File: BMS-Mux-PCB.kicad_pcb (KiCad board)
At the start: 2 copper layers, 113.5 x 88 mm, 54 parts, among them J1 Conn_02x08_Counter_Clockwise, J2 Conn_02x08_Counter_Clockwise, J3 Conn_02x09_Top_Bottom, J4 Conn_01x18, J5 Conn_01x02, J6 Conn_02x10_Odd_Even, Q1 BSS123, Q2 BSS123, U1 74CBTLV3257, U2 74CBTLV3257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

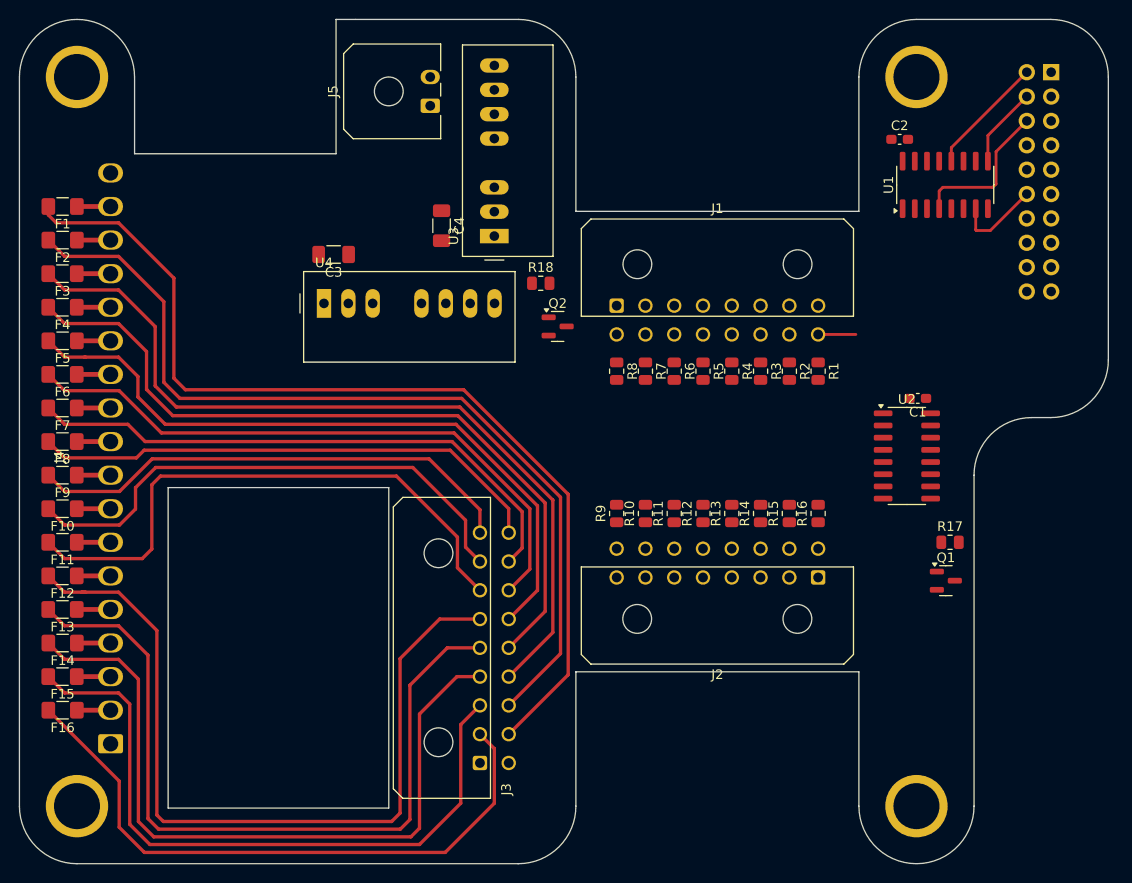
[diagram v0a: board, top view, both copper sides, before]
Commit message: changed connector orientation and halfway routed
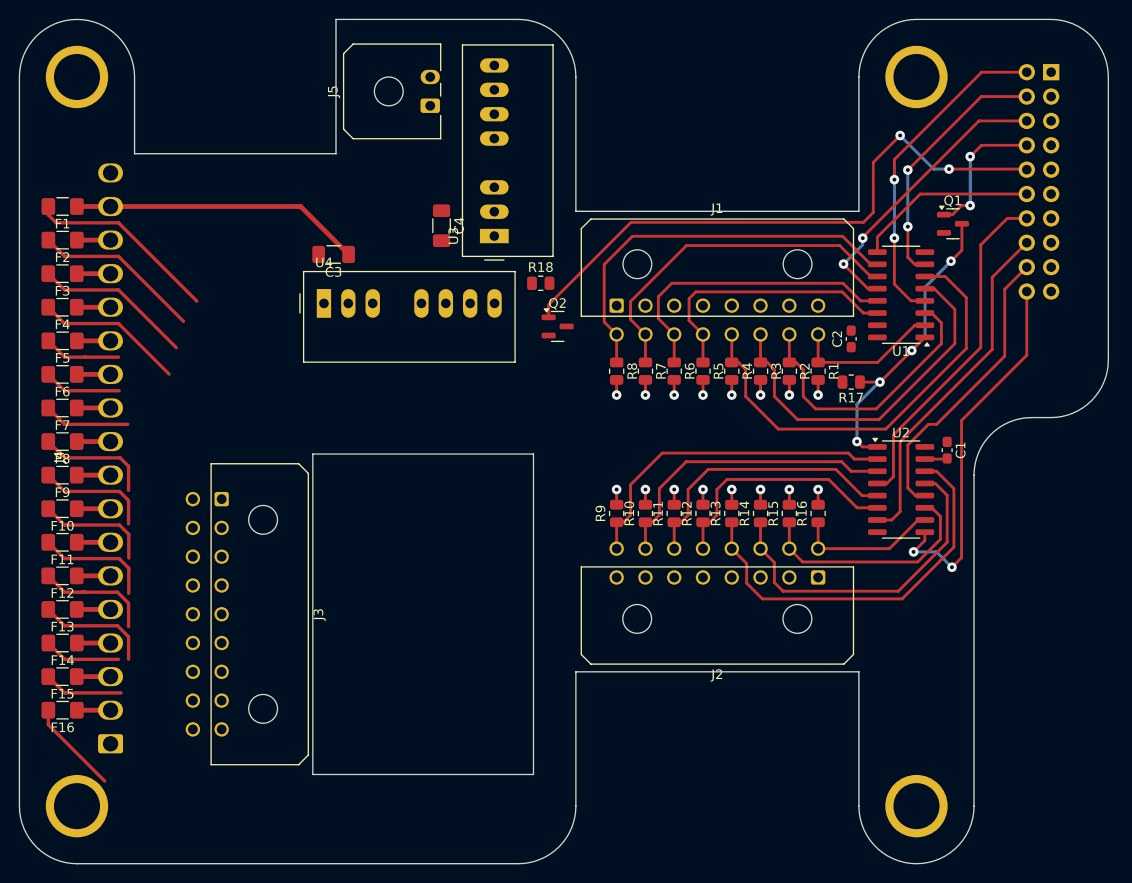
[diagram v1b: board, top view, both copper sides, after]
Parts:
- moved J3 38.5 mm to (85.6, 99.5), turned to -90 degrees
- moved Q1 37.2 mm to (161.8, 70.8)
- moved C2 21.4 mm to (151.2, 82.8), turned to 90 degrees
- moved R17 19.6 mm to (151.2, 87.3), turned to 180 degrees
- moved U1 12.3 mm to (156.4, 78.2), turned to 180 degrees
- moved C1 6.21 mm to (161.2, 94.4), turned to -90 degrees
- moved U2 3.55 mm to (156.4, 98.5)
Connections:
- J3 pad 1: GND -> /BATT_15
- J3 pad 10: unconnected-(J3-Pin_10-Pad10) -> /BATT_16
- J3 pad 11: /BATT_16 -> /BATT_14
- J3 pad 12: /BATT_15 -> /BATT_12
- J3 pad 13: /BATT_14 -> /BATT_10
- J3 pad 14: /BATT_13 -> /BATT_8
- J3 pad 15: /BATT_12 -> /BATT_6
- J3 pad 16: /BATT_11 -> /BATT_4
- J3 pad 17: /BATT_10 -> /BATT_2
- J3 pad 18: /BATT_9 -> unconnected-(J3-Pin_18-Pad18)
- J3 pad 2: /BATT_1 -> /BATT_13
- J3 pad 3: /BATT_2 -> /BATT_11
- J3 pad 4: /BATT_3 -> /BATT_9
- J3 pad 5: /BATT_4 -> /BATT_7
- J3 pad 7: /BATT_6 -> /BATT_3
- J3 pad 8: /BATT_7 -> /BATT_1
- J3 pad 9: /BATT_8 -> GND
- U1 pad 10: /SENS_4 -> /SENS_8
- U1 pad 11: /SENS_3 -> /SENS_7
- U1 pad 12: /GPIO1_ADC -> /GPIO3_ADC
- U1 pad 13: /SENS_2 -> /SENS_6
- U1 pad 14: /SENS_1 -> /SENS_5
- U1 pad 2: /SENS_5 -> /SENS_1
- U1 pad 3: /SENS_6 -> /SENS_2
- U1 pad 4: /GPIO3_ADC -> /GPIO1_ADC
- U1 pad 5: /SENS_7 -> /SENS_3
- U1 pad 6: /SENS_8 -> /SENS_4
- U1 pad 7: /GPIO6_ADC -> /GPIO2_ADC
- U1 pad 9: /GPIO2_ADC -> /GPIO6_ADC
- U2 pad 10: /SENS_14 -> /SENS_16
- U2 pad 11: /SENS_13 -> /SENS_15
- U2 pad 12: /GPIO10_ADC -> /GPIO9_ADC
- U2 pad 13: /SENS_16 -> /SENS_14
- U2 pad 14: /SENS_15 -> /SENS_13
- U2 pad 9: /GPIO9_ADC -> /GPIO10_ADC
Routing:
- net /BATT_16: track 100.8 -> 20.1 mm
- net /BATT_15: track 93.3 -> 17.6 mm
- net /BATT_5: track 85.4 -> 12.4 mm
- net /BATT_14: track 86.3 -> 16.5 mm
- net /BATT_4: track 80.5 -> 11.9 mm
- net /BATT_3: track 75.9 -> 8.03 mm
- net /BATT_12: track 72.5 -> 8.13 mm
- net /BATT_13: track 79.2 -> 15.5 mm
- net /GPIO6_EN: track 0.00 -> 63.0 mm, vias 0 -> 2
- net /BATT_2: track 70.4 -> 8.30 mm
- net /BATT_11: track 65.4 -> 8.10 mm
- net /BATT_1: track 65.4 -> 9.82 mm
- net /BATT_10: track 59.7 -> 9.00 mm
- net /BATT_6: track 60.0 -> 12.1 mm
- net /SENS_4: track 0.00 -> 45.9 mm
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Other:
- outline, holes or cut-outs redrawn

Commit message: V1 almost done - touching up silkscreen
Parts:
- moved F1 52.5 mm to (69.3, 121.5)
- moved F16 52.5 mm to (69.3, 69.0)
- moved F15 45.5 mm to (69.3, 72.5)
- moved F2 45.5 mm to (69.3, 118.0)
- moved F3 38.5 mm to (69.3, 114.5)
- moved F14 38.5 mm to (69.3, 76.0)
- moved F13 31.5 mm to (69.3, 79.5)
- moved F4 31.5 mm to (69.3, 111.0)
- moved F12 24.5 mm to (69.3, 83.0)
- moved F5 24.5 mm to (69.3, 107.5)
- moved F11 17.5 mm to (69.3, 86.5)
- moved F6 17.5 mm to (69.3, 104.0)
- moved C3 16.8 mm to (80.8, 70.8), turned to -90 degrees
- moved U4 13.3 mm to (85.0, 72.0)
- moved J3 10.5 mm to (85.0, 89.0)
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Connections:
- F1 pad 1: +V_BAT -> Net-(J4-Pin_2)
- F1 pad 2: /BATT_16 -> /BATT_1
- F10 pad 1: Net-(J4-Pin_8) -> Net-(J4-Pin_11)
- F10 pad 2: /BATT_7 -> /BATT_10
- F11 pad 1: Net-(J4-Pin_7) -> Net-(J4-Pin_12)
- F11 pad 2: /BATT_6 -> /BATT_11
- F12 pad 1: Net-(J4-Pin_6) -> Net-(J4-Pin_13)
- F12 pad 2: /BATT_5 -> /BATT_12
- F13 pad 1: Net-(J4-Pin_5) -> Net-(J4-Pin_14)
- F13 pad 2: /BATT_4 -> /BATT_13
- F14 pad 1: Net-(J4-Pin_4) -> Net-(J4-Pin_15)
- F14 pad 2: /BATT_3 -> /BATT_14
- F15 pad 1: Net-(J4-Pin_3) -> Net-(J4-Pin_16)
- F15 pad 2: /BATT_2 -> /BATT_15
- F16 pad 1: Net-(J4-Pin_2) -> +V_BAT
- F16 pad 2: /BATT_1 -> /BATT_16
- F2 pad 1: Net-(J4-Pin_16) -> Net-(J4-Pin_3)
- F2 pad 2: /BATT_15 -> /BATT_2
- F3 pad 1: Net-(J4-Pin_15) -> Net-(J4-Pin_4)
- F3 pad 2: /BATT_14 -> /BATT_3
- F4 pad 1: Net-(J4-Pin_14) -> Net-(J4-Pin_5)
- F4 pad 2: /BATT_13 -> /BATT_4
- F5 pad 1: Net-(J4-Pin_13) -> Net-(J4-Pin_6)
- F5 pad 2: /BATT_12 -> /BATT_5
- F6 pad 1: Net-(J4-Pin_12) -> Net-(J4-Pin_7)
- F6 pad 2: /BATT_11 -> /BATT_6
- F7 pad 1: Net-(J4-Pin_11) -> Net-(J4-Pin_8)
- F7 pad 2: /BATT_10 -> /BATT_7
- F8 pad 1: Net-(J4-Pin_10) -> Net-(J4-Pin_9)
- F8 pad 2: /BATT_9 -> /BATT_8
- F9 pad 1: Net-(J4-Pin_9) -> Net-(J4-Pin_10)
- F9 pad 2: /BATT_8 -> /BATT_9
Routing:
- net +3V3: track 25.4 -> 142.2 mm, vias 16 -> 14
- net /EN_SIG: track 0.00 -> 29.3 mm
- net GND: track 2.35 -> 29.8 mm, vias 0 -> 3
- net +V_BAT: track 30.4 -> 13.6 mm
- net /BATT_11: track 8.10 -> 24.5 mm
- net /BATT_1: track 9.82 -> 25.8 mm
- net /BATT_3: track 8.03 -> 23.2 mm
- net /BATT_12: track 8.13 -> 22.2 mm
- net /BATT_15: track 17.6 -> 31.4 mm
- net /BATT_2: track 8.30 -> 20.9 mm
- net /BATT_13: track 15.5 -> 27.6 mm
- net /BATT_10: track 9.00 -> 18.9 mm
- net /BATT_14: track 16.5 -> 26.2 mm
- net /BATT_16: track 20.1 -> 29.3 mm
- net /BATT_9: track 11.9 -> 20.5 mm
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- added copper zone on F.Cu, net +V_BAT
- added copper zone on B.Cu, net GND
- added copper zone on F.Cu, net GND
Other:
- outline, holes or cut-outs redrawn
- board text added: "1"
- board text added: "12V ISOLATED"
- board text added: "2"
- board text added: "3"
- board text added: "4"
- board text added: "BMS AUX BOARD"
- board text added: "G"
- board text added: "HV ISO ->"
- board text added: "PCB CONN FRONT VIEW"
- board text added: "SENS"
- board text added: "SENS 1-8 IN"
- board text added: "SENS 9-16 IN"
- board text added: "V1"
- board text added: "VOLTAGE SENSE IN"
- board text added: "VSENSE"
- board text added: "X"

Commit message: added pdfs and finalised V1
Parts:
- added G***: LOGO, LOGO, F.Cu at (108.9, 127.7)
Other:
- board text added: "BMS MUX BOARD"
- board text added: "Made by @Amrlxyz (Github)"
- board text added: "TEMP"
- board text added: "TEMP 1-8 INPUT"
- board text added: "TEMP 9-16 INPUT"
- board text removed: "BMS AUX BOARD"
- board text removed: "SENS"
- board text removed: "SENS 1-8 IN"
- board text removed: "SENS 9-16 IN"

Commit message: added some small changes for manufacturing purposes and gerber file generated
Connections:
- net Net-(J5-Pin_1) renamed /+12V_ISO
- net Net-(J5-Pin_2) renamed /GND_ISO
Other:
- board text added: "+"

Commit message: fixed the gpio pin name number (minor fix)
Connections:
- net /GPIO5_SW renamed /GPIO4_SW
- net /GPIO6_EN renamed /GPIO5_EN
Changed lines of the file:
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@@
 	(net 56 "/GPIO2_ADC")
 	(net 57 "/GPIO8_ADC")
-	(net 58 "/GPIO6_EN")
-	(net 59 "/GPIO5_SW")
+	(net 58 "/GPIO5_EN")
+	(net 59 "/GPIO4_SW")
 	(net 60 "/GPIO6_ADC")
 	(net 61 "/GPIO1_ADC")
@@
 			(layers "F.Cu" "F.Paste" "F.Mask")
 			(roundrect_rratio 0.25)
-			(net 58 "/GPIO6_EN")
+			(net 58 "/GPIO5_EN")
 			(pinfunction "G")
 			(pintype "input")
@@
 			(layers "F.Cu" "F.Paste" "F.Mask")
 			(roundrect_rratio 0.25)
-			(net 59 "/GPIO5_SW")
+			(net 59 "/GPIO4_SW")
 			(pinfunction "G")
 			(pintype "input")
@@
 			)
 			(remove_unused_layers no)
-			(net 59 "/GPIO5_SW")
+			(net 59 "/GPIO4_SW")
 			(pinfunction "Pin_8")
 			(pintype "passive")
@@
 			)
 			(remove_unused_layers no)
-			(net 58 "/GPIO6_EN")
+			(net 58 "/GPIO5_EN")
 			(pinfunction "Pin_10")
 			(pintype "passive")
